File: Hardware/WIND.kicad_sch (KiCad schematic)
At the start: 2 parts, among them J3 Wind

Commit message: update of directory
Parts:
- added C4, C7, C9: 100nF, Capacitor_THT:C_Rect_L7.0mm_W2.0mm_P5.00mm, symbol Device:C
- added R10, R11, R12, R15, R5: 10k, Resistor_THT:R_Axial_DIN0204_L3.6mm_D1.6mm_P5.08mm_Horizontal, symbol Device:R
- added RV1: R_Potentiometer, Potentiometer_THT:Potentiometer_Bourns_3266Y_Vertical, symbol Device:R_Potentiometer
- added U5: 74HC123, Package_DIP:DIP-16_W7.62mm_Socket, symbol 74xx:74HC123
- added U6: LM358, Package_DIP:DIP-8_W7.62mm_Socket, symbol Amplifier_Operational:LM358
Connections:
- net +5V: now also C9.1, R5.1, RV1.1, U6.8 (V+)
- net GND: now also C7.2, C9.2, R15.1, RV1.3, U5.3 (Clr), U6.4 (V-)
- net OUT renamed RAW_DATA
- net RAW_DATA: now also U5.2 (B)
- new net: R10.1, U5.13 (Q)
- new net: C4.2, U5.14 (Cext)
- new net: C4.1, R5.2, U5.15 (RCext)
- new net: C7.1, R10.2, R11.1
- new net: RV1.2, U6.2 (-)
- new net: R11.2, R12.1, U6.3 (+)
- new net Wind_interrupt: R12.2, R15.2, U6.1
- no-connect marks 0 -> 2

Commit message: Update of PCB
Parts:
- R10, R11, R12, R15, R4, R5: footprint Resistor_THT:R_Axial_DIN0204_L3.6mm_D1.6mm_P5.08mm_Horizontal -> Resistor_THT:R_Axial_DIN0207_L6.3mm_D2.5mm_P7.62mm_Horizontal

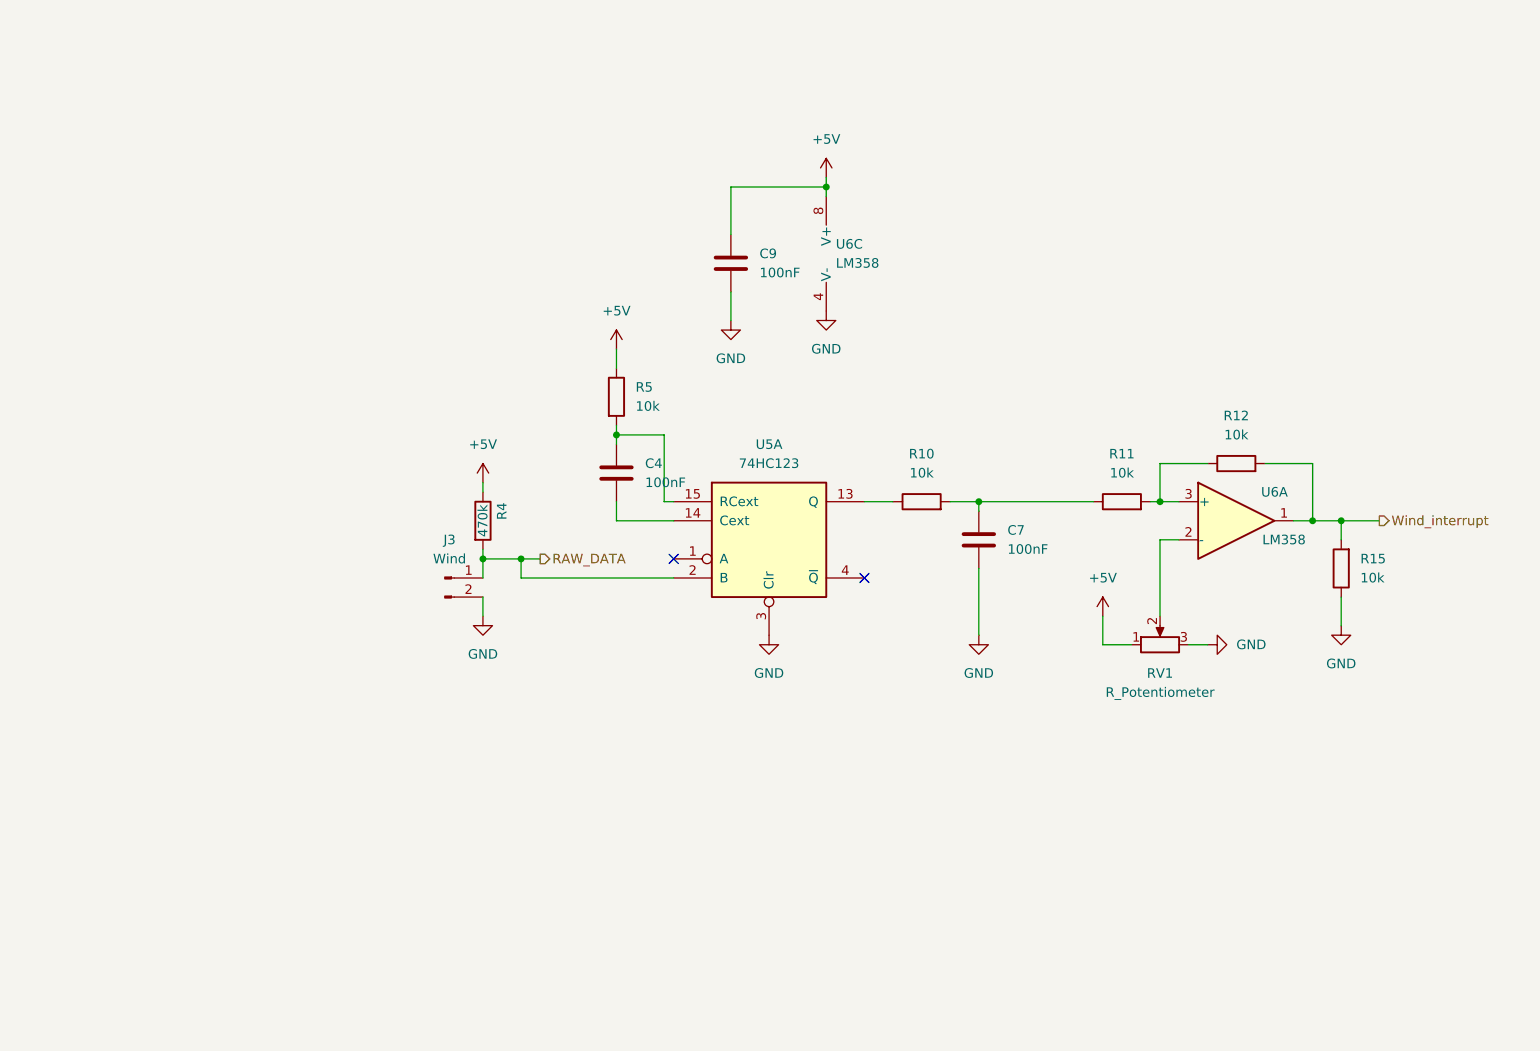
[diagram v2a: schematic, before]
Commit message: Update PCB of Motor controller - version sent on production (debug purpose)
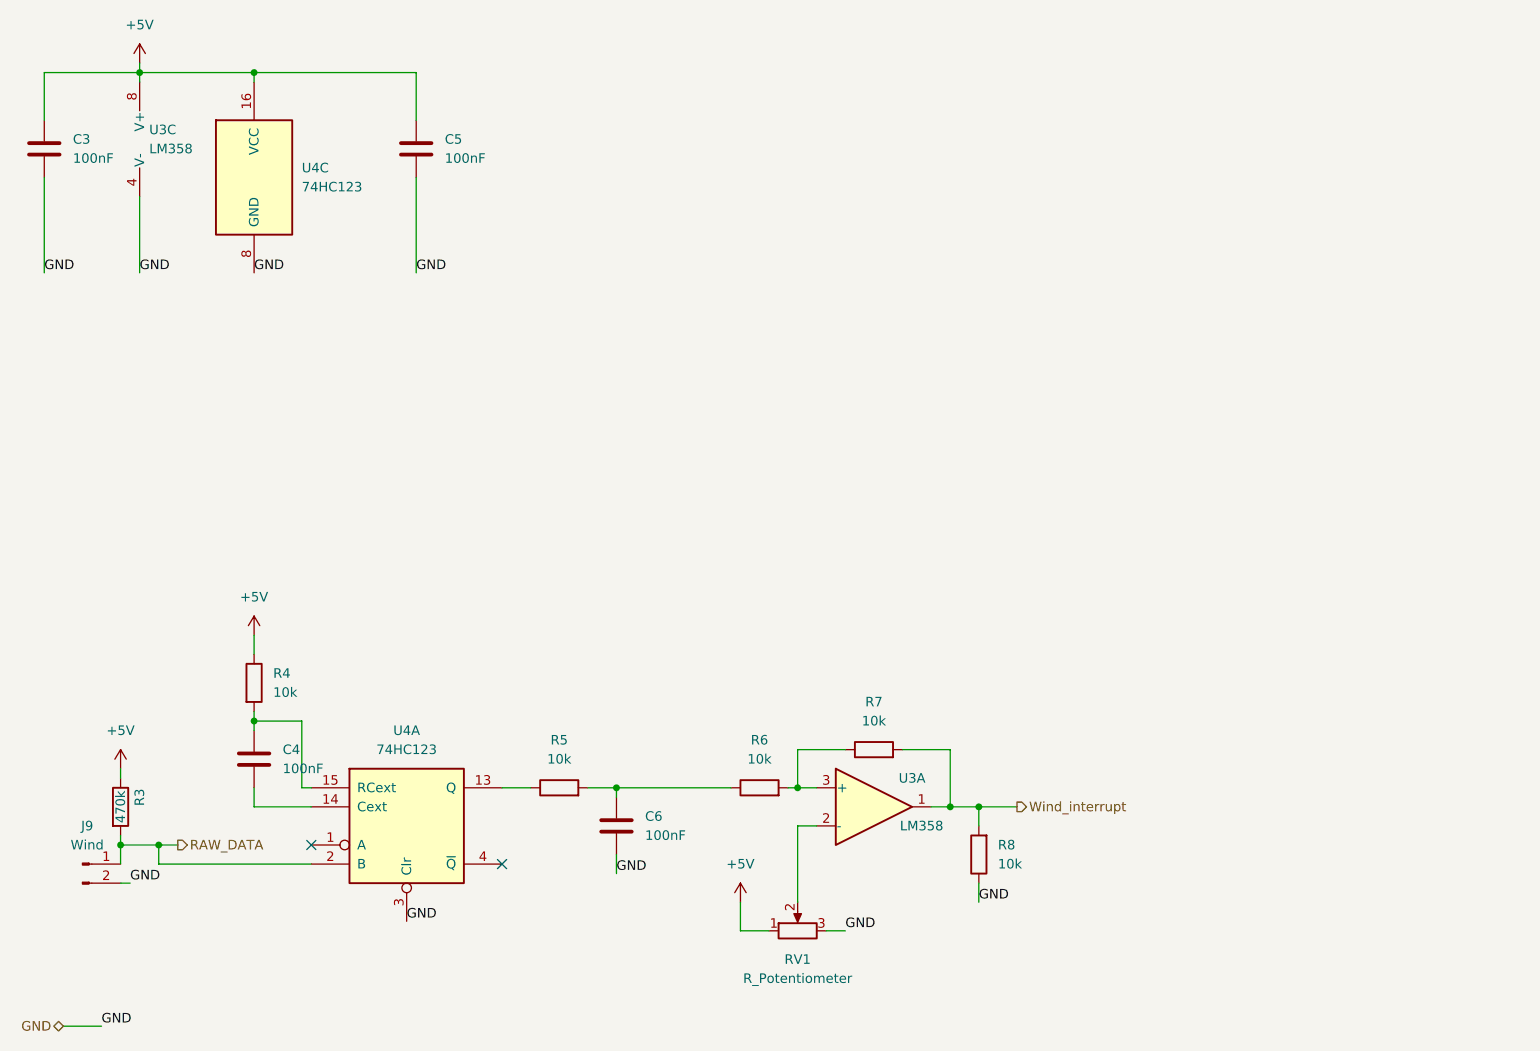
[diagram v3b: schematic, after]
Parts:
- added C5: 100nF, Capacitor_THT:C_Rect_L7.0mm_W2.0mm_P5.00mm, symbol Device:C
- added unit 3 of U4
- renumbered C9 to C3, C7 to C6, J3 to J9, R4 to R3, R5 to R4, R10 to R5, R11 to R6, R12 to R7, R15 to R8, U6 to U3, U5 to U4
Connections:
- net +5V: now also C5.1, U4.16 (VCC)
- net GND: now also C5.2, U4.8 (GND)
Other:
- moved on the sheet: C3, C4, C6, J9, R3, R4, R5, R6, R7, R8, RV1, U3A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
